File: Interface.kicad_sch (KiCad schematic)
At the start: 62 parts, among them U2 WE-TVS-82400102, U3 THVD1400D, U4 SN74LVC2G14DBV, U5 SN74LVC2G14DBV, U6 WE-TVS-82400102, U7 TLP2310, U8 SN74LVC2G14DBV, U9 TLP2310

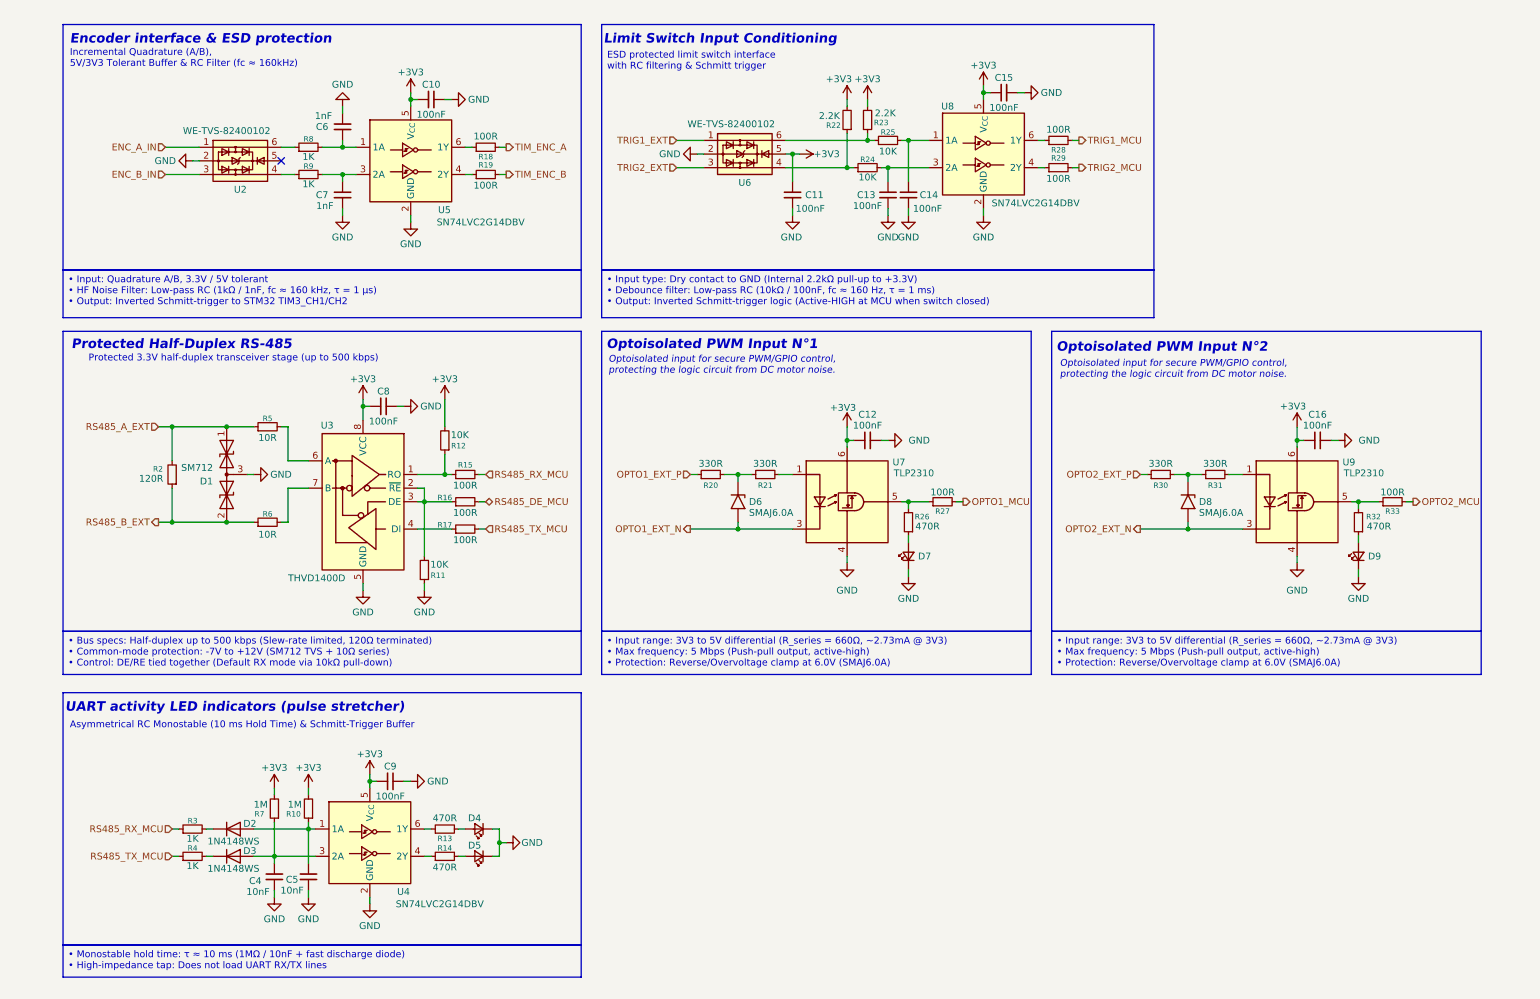
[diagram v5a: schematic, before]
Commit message: refactor(schematic): migrate MCU to LQFP48 and finalize pinout mapping
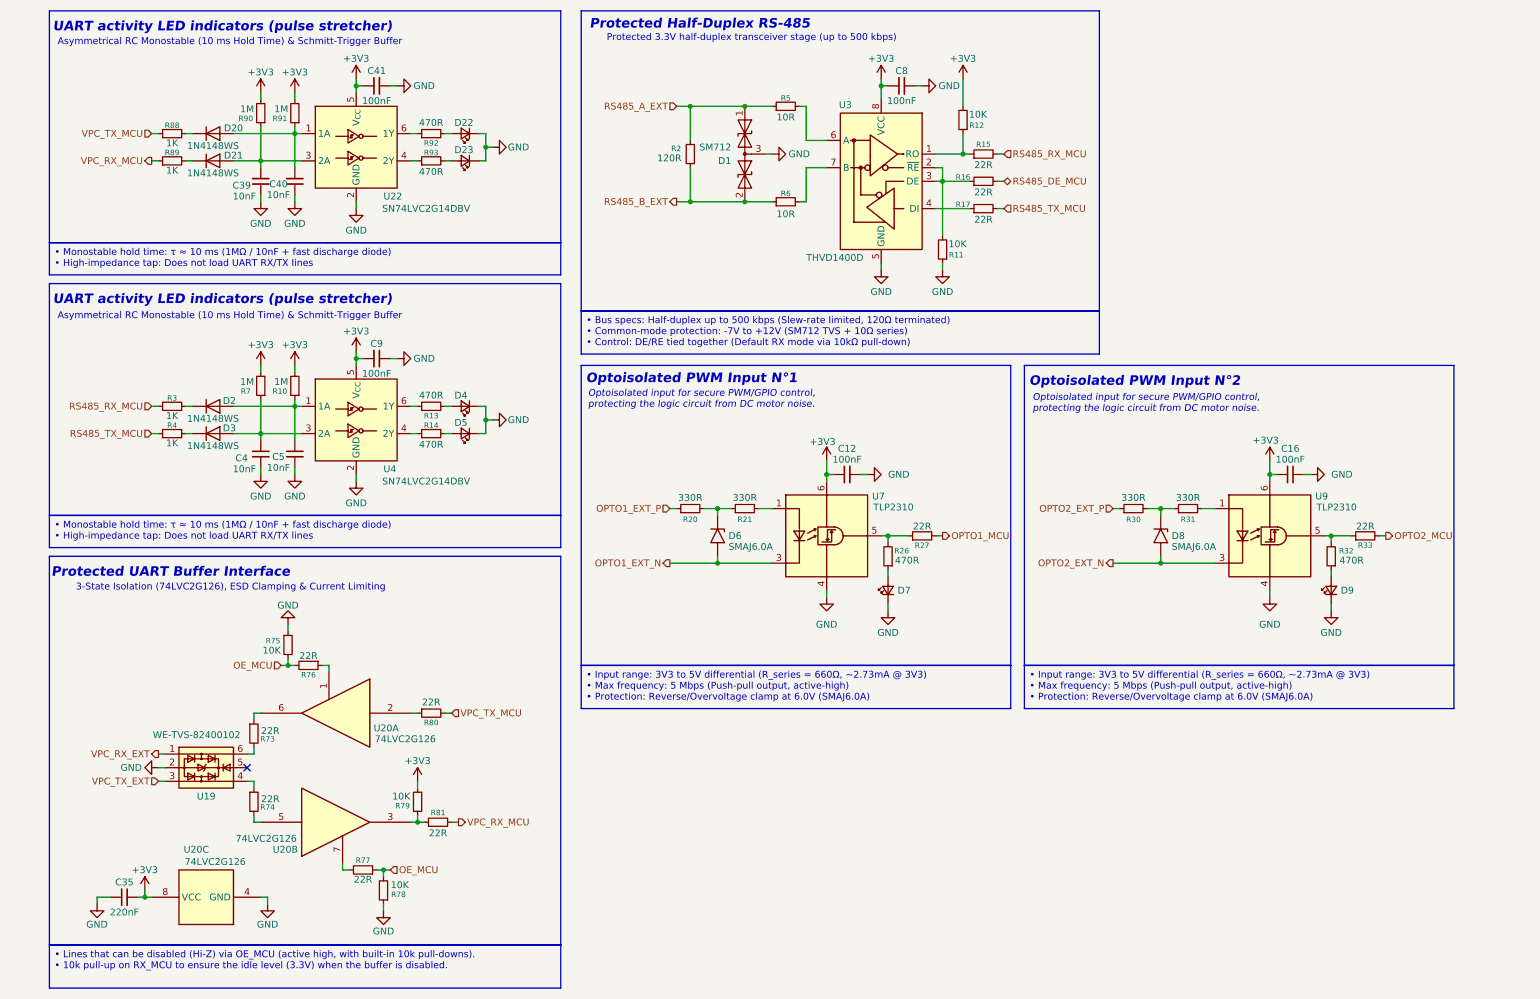
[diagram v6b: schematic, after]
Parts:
- removed C10, C11, C13, C14, C15: 100nF, Capacitor_SMD:C_0603_1608Metric, symbol Device:C_Small
- removed C6, C7: 1nF, Capacitor_SMD:C_0603_1608Metric, symbol Device:C_Small
- removed R18, R19, R28, R29: 100R, Resistor_SMD:R_0603_1608Metric, symbol Device:R_Small
- removed R22, R23: 2.2K, Resistor_SMD:R_0603_1608Metric, symbol Device:R_Small
- removed R24, R25: 10K, Resistor_SMD:R_0603_1608Metric, symbol Device:R_Small
- removed R8, R9: 1K, Resistor_SMD:R_0603_1608Metric, symbol Device:R_Small
- removed U2, U6: WE-TVS-82400102, Package_TO_SOT_SMD:SOT-23-6, symbol Power_Protection:WE-TVS-82400102
- removed U5, U8: SN74LVC2G14DBV, Package_TO_SOT_SMD:SOT-23-6, symbol 74xGxx:SN74LVC2G14DBV
- added C35: 220nF, Capacitor_SMD:C_0603_1608Metric, symbol Device:C_Small
- added C39, C40: 10nF, Capacitor_SMD:C_0603_1608Metric, symbol Device:C_Small
- added C41: 100nF, Capacitor_SMD:C_0603_1608Metric, symbol Device:C_Small
- added D20, D21: 1N4148WS, Diode_SMD:D_SOD-323, symbol Diode:1N4148WS
- added D22, D23: LED_Small, LED_SMD:LED_0603_1608Metric, symbol Device:LED_Small
- added R73, R74, R76, R77, R80, R81: 22R, Resistor_SMD:R_0603_1608Metric, symbol Device:R_Small
- added R75, R78, R79: 10K, Resistor_SMD:R_0603_1608Metric, symbol Device:R_Small
- added R88, R89: 1K, Resistor_SMD:R_0603_1608Metric, symbol Device:R_Small
- added R90, R91: 1M, Resistor_SMD:R_0603_1608Metric, symbol Device:R_Small
- added R92, R93: 470R, Resistor_SMD:R_0603_1608Metric, symbol Device:R_Small
- added U19: WE-TVS-82400102, Package_TO_SOT_SMD:SOT-23-6, symbol Power_Protection:WE-TVS-82400102
- added U20: 74LVC2G126, Package_SO:VSSOP-8_2.3x2mm_P0.5mm, symbol 74xGxx:74LVC2G126
- added U22: SN74LVC2G14DBV, Package_TO_SOT_SMD:SOT-23-6, symbol 74xGxx:SN74LVC2G14DBV
- R15, R16, R17, R27, R33: value 100R -> 22R
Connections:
- net +3V3: now also C35.1, C41.1, R79.2, R90.2, R91.2, U20.8 (VCC), U22.5 (V_{CC})
- net GND: now also C35.2, C39.1, C40.1, C41.2, D22.1 (K), D23.1 (K), R75.1, R78.1, U19.2, U20.4 (GND), U22.2 (GND)
- new net: R80.1, U20.2
- new net: R77.2, U20.7
- new net: R74.1, U19.4
- new net: R74.2, U20.5
- new net: R92.1, U22.6 (1Y)
- new net: D22.2 (A), R92.2
- new net: R93.1, U22.4 (2Y)
- new net: D23.2 (A), R93.2
- new net: C39.2, D21.2 (A), R90.1, U22.3 (2A)
- new net: R73.1, U20.6
- new net: R73.2, U19.6
- new net: C40.2, D20.2 (A), R91.1, U22.1 (1A)
- new net: D20.1 (K), R88.2
- new net: D21.1 (K), R89.2
- new net: R79.1, R81.1, U20.3
- new net: R76.1, U20.1
- new net OE_MCU: R75.2, R76.2, R77.1, R78.2
- new net VPC_RX_EXT: U19.1
- new net VPC_RX_MCU: R81.2, R89.1
- new net VPC_TX_EXT: U19.3
- new net VPC_TX_MCU: R80.2, R88.1
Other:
- note added: "3-State Isolation (74LVC2G126), ESD Clamping & Current Limiting"
- note added: "Protected UART Buffer Interface"
- note removed: "ESD protected limit switch interface with RC filtering & Schmitt trigger"
- note removed: "Encoder interface & ESD protection"
- note removed: "Incremental Quadrature (A/B), 5V/3V3 Tolerant Buffer & RC Filter (fc ≈ 160kHz)"
- note removed: "Limit Switch Input Conditioning"
- moved on the sheet: C12, C16, C4, C5, C8, C9, D1, D2, D3, D4, D5, D6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

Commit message: feat : add SMLVN6RGB status LED stage with balanced 3.3V ballast resistors
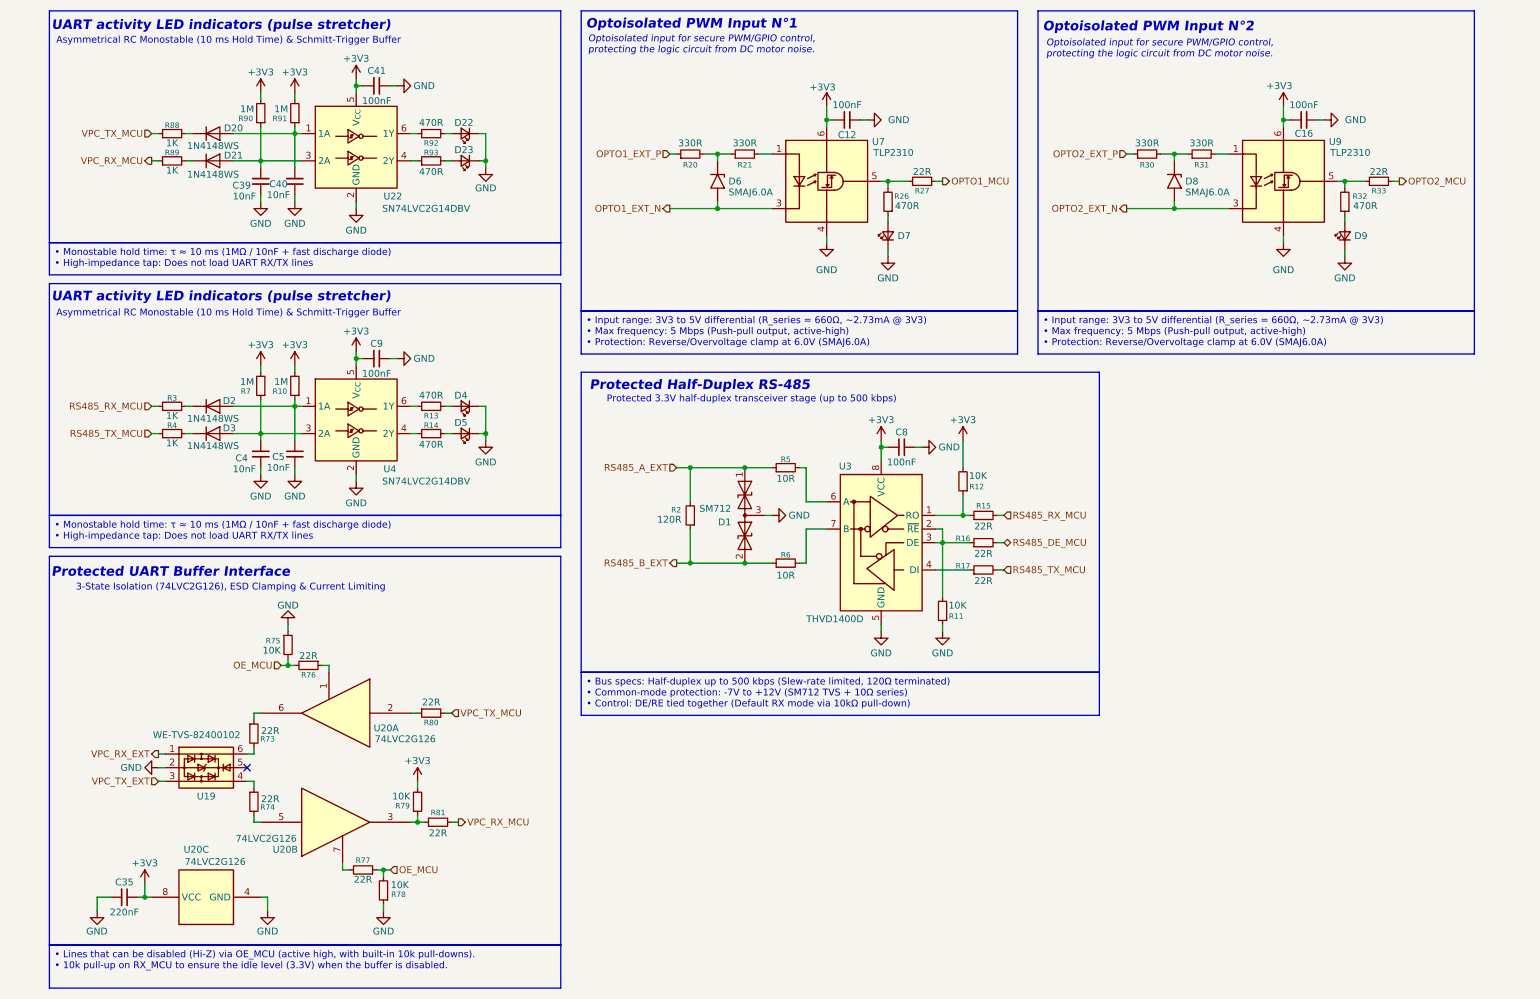
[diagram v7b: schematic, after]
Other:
- moved on the sheet: C12, C16, C8, D1, D6, D7, D8, D9, R11, R12, R15, R16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

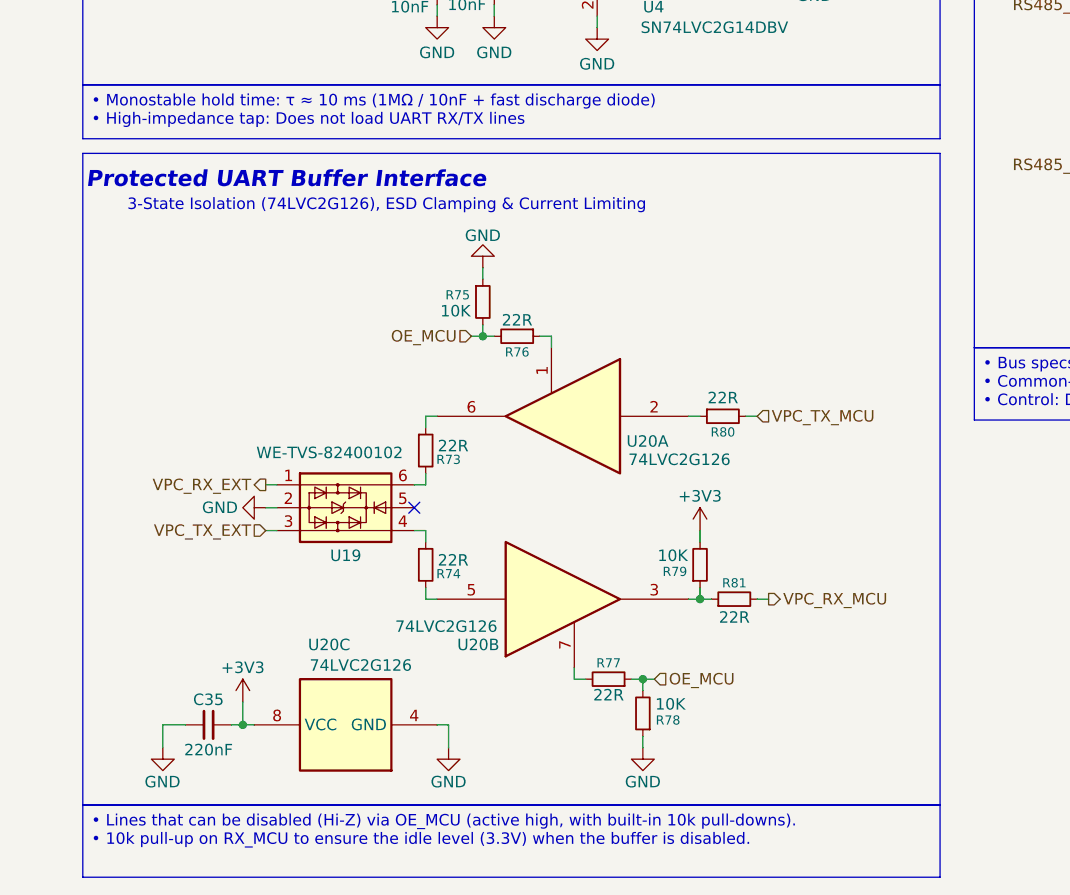
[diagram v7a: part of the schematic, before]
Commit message: feat: switch to JST-GH connectors and add TPD4E05U06 TVS protection for SPI/I2C
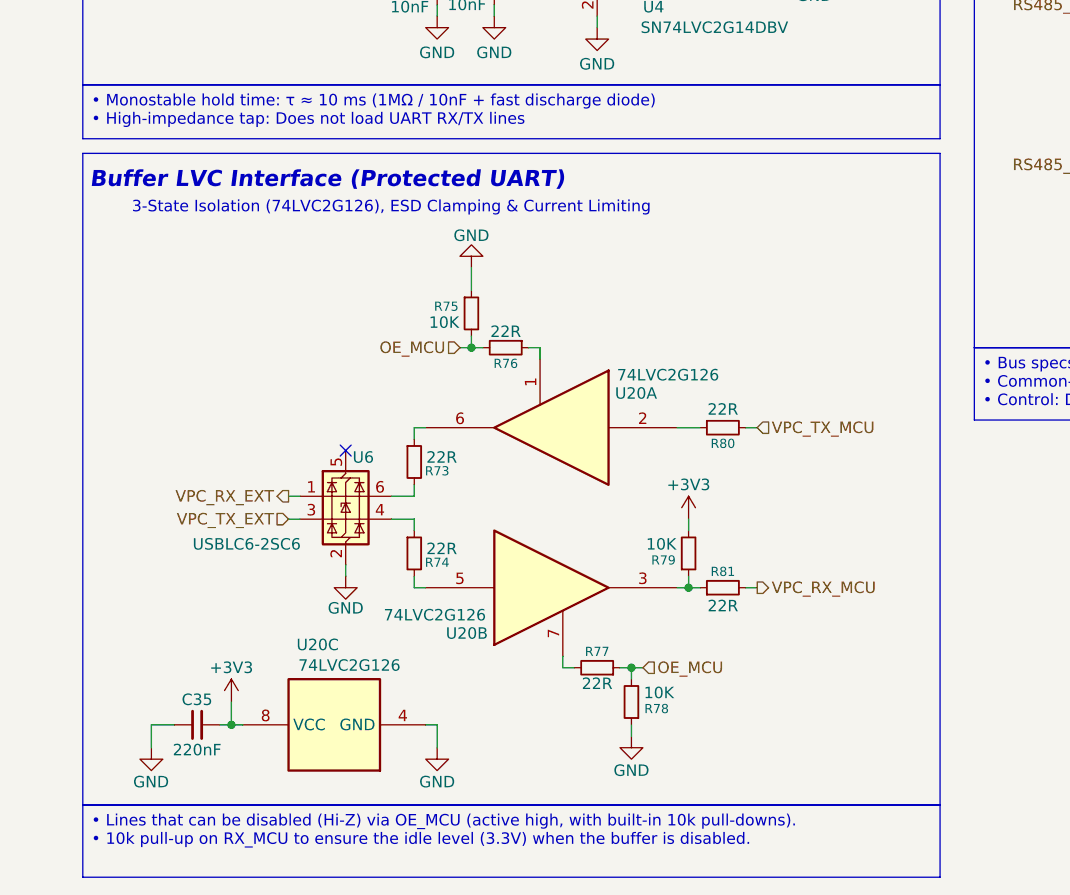
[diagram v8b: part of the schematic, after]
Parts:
- removed U19: WE-TVS-82400102, Package_TO_SOT_SMD:SOT-23-6, symbol Power_Protection:WE-TVS-82400102
- added U6: USBLC6-2SC6, Package_TO_SOT_SMD:SOT-23-6, symbol Power_Protection:USBLC6-2SC6
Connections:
- net GND: now also U6.2 (GND)
- net VPC_RX_EXT: now also U6.1 (I/O1)
- net VPC_TX_EXT: now also U6.3 (I/O2)
- net at R74.1: now also U6.4 (I/O2)
- net at R73.2: now also U6.6 (I/O1)
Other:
- note added: "Buffer LVC Interface (Protected UART)"
- note removed: "Protected UART Buffer Interface"
- moved on the sheet: C35, R73, R74, R75, R76, R77, R78, R79, R80, R81, U20A, U20B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
